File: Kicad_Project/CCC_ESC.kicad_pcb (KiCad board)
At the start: 4 copper layers, 99.9 x 82.6 mm, 160 parts, among them J1 Conn_01x07, J2 Conn_01x06, J3 Conn_01x06, J4 Conn_01x06, SW1 Conn_01x02, U1 NCP5183 / TF2190-TAH, U2 NCP5183 / TF2190-TAH, U3 NCP5183 / TF2190-TAH, U4 NCS20034DR2G, U5 STM32F401CCU6_Balckpill, U6 PQDE6W-Q110 / RD5-110S12W, U7 TO220_replacement_module

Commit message: initial layout approach
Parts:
- removed CX1, CX2, CX3, CX4, CX5, CX6, CX7, CX8: 470uF, CCC_ESC_Custom_parts:CAP_Polaryzed
- removed CX18, CX19, CX20, CX21, CX22, CX23, CX24, CX25, CX26, CX27, CX28, CX29, CX30, CX31, CX32: 4.7uF, Capacitor_SMD:C_1210_3225Metric
- removed PH2 (x2): PhasePad, TestPoint:TestPoint_THTPad_D4.0mm_Drill2.0mm
- removed TpVS1: TestPoint, TestPoint:TestPoint_THTPad_D2.0mm_Drill1.0mm
- added CD3: 4.7uF, Capacitor_SMD:C_1210_3225Metric, F.Cu at (86.2, 72.6)
- added CD4: 4.7uF, Capacitor_SMD:C_1210_3225Metric, F.Cu at (114.0, 72.6)
- added CD5: 4.7uF, Capacitor_SMD:C_1210_3225Metric, F.Cu at (118.2, 72.6)
- added CD6: 4.7uF, Capacitor_SMD:C_1210_3225Metric, F.Cu at (146.0, 72.6)
- added CS1: C, Capacitor_SMD:C_0805_2012Metric, F.Cu at (53.6, 81.6)
- added CS2: C, Capacitor_SMD:C_0805_2012Metric, F.Cu at (85.8, 81.7)
- added CS3: C, Capacitor_SMD:C_0805_2012Metric, F.Cu at (117.8, 81.7)
- added CX17: 4.7uF, Capacitor_SMD:C_1210_3225Metric, F.Cu at (67.2, 51.1)
- added NT3: NetTie_2, NetTie:NetTie-2_SMD_Pad0.5mm, F.Cu at (102.6, 88.5)
- added NT4: NetTie_2, NetTie:NetTie-2_SMD_Pad0.5mm, F.Cu at (102.6, 90.6)
- added NT5: NetTie_2, NetTie:NetTie-2_SMD_Pad0.5mm, F.Cu at (134.6, 88.5)
- added NT6: NetTie_2, NetTie:NetTie-2_SMD_Pad0.5mm, F.Cu at (134.6, 90.6)
- added PHA_1: PhasePad, TestPoint:my_2mm_slot, F.Cu at (59.3, 72.4)
- added PHA_2: PhasePad, TestPoint:my_2mm_slot, F.Cu at (76.1, 72.4)
- added PHB_1: PhasePad, TestPoint:my_2mm_slot, F.Cu at (91.8, 72.4)
- added PHB_2: PhasePad, TestPoint:my_2mm_slot, F.Cu at (108.3, 72.4)
- added PHC_1: PhasePad, TestPoint:my_2mm_slot, F.Cu at (123.6, 72.4)
- added PHC_2: PhasePad, TestPoint:my_2mm_slot, F.Cu at (140.3, 72.4)
- added QB1: NVMTSC4D3N15MC, Package_DFN_QFN:DFNW-8_L8.3-W8.4-P2.00-BL, F.Cu at (91.4, 64.6)
- added QB2: NVMTSC4D3N15MC, Package_DFN_QFN:DFNW-8_L8.3-W8.4-P2.00-BL, F.Cu at (91.3, 80.6)
- added QB3: NVMTSC4D3N15MC, Package_DFN_QFN:DFNW-8_L8.3-W8.4-P2.00-BL, F.Cu at (112.2, 64.6)
- added QB4: NVMTSC4D3N15MC, Package_DFN_QFN:DFNW-8_L8.3-W8.4-P2.00-BL, F.Cu at (101.7, 80.6)
- added QB5: NVMTSC4D3N15MC, Package_DFN_QFN:DFNW-8_L8.3-W8.4-P2.00-BL, F.Cu at (101.6, 64.6)
- added QB6: NVMTSC4D3N15MC, Package_DFN_QFN:DFNW-8_L8.3-W8.4-P2.00-BL, F.Cu at (112.1, 80.6)
- added QC1: NVMTSC4D3N15MC, Package_DFN_QFN:DFNW-8_L8.3-W8.4-P2.00-BL, F.Cu at (123.3, 64.6)
- added QC2: NVMTSC4D3N15MC, Package_DFN_QFN:DFNW-8_L8.3-W8.4-P2.00-BL, F.Cu at (123.4, 80.6)
- added QC3: NVMTSC4D3N15MC, Package_DFN_QFN:DFNW-8_L8.3-W8.4-P2.00-BL, F.Cu at (133.7, 64.6)
- added QC4: NVMTSC4D3N15MC, Package_DFN_QFN:DFNW-8_L8.3-W8.4-P2.00-BL, F.Cu at (133.8, 80.6)
- added QC5: NVMTSC4D3N15MC, Package_DFN_QFN:DFNW-8_L8.3-W8.4-P2.00-BL, F.Cu at (144.0, 64.6)
- added QC6: NVMTSC4D3N15MC, Package_DFN_QFN:DFNW-8_L8.3-W8.4-P2.00-BL, F.Cu at (144.1, 80.6)
- added REF**: CP_Radial_D18.0mm_P7.50mm, Capacitor_THT:CP_Radial_D18.0mm_P7.50mm, F.Cu at (57.3, 40.3)
- added REF**1: CP_Radial_D18.0mm_P7.50mm, Capacitor_THT:CP_Radial_D18.0mm_P7.50mm, F.Cu at (77.3, 40.3)
- added REF**2: CP_Radial_D18.0mm_P7.50mm, Capacitor_THT:CP_Radial_D18.0mm_P7.50mm, F.Cu at (97.3, 40.3)
- added REF**3: CP_Radial_D18.0mm_P7.50mm, Capacitor_THT:CP_Radial_D18.0mm_P7.50mm, F.Cu at (117.3, 40.3)
- added REF**4: CP_Radial_D18.0mm_P7.50mm, Capacitor_THT:CP_Radial_D18.0mm_P7.50mm, F.Cu at (137.3, 40.3)
- added RG10: 15R, Resistor_SMD:R_0603_1608Metric, F.Cu at (88.3, 87.2)
- added RG11: 15R, Resistor_SMD:R_0603_1608Metric, F.Cu at (96.6, 84.7)
- added RG12: 15R, Resistor_SMD:R_0603_1608Metric, F.Cu at (106.8, 84.6)
- added RG13: 15R, Resistor_SMD:R_0603_1608Metric, F.Cu at (117.9, 65.2)
- added RG14: 15R, Resistor_SMD:R_0603_1608Metric, F.Cu at (128.5, 67.9)
- added RG15: 15R, Resistor_SMD:R_0603_1608Metric, F.Cu at (138.8, 67.9)
- added RG16: 15R, Resistor_SMD:R_0603_1608Metric, F.Cu at (120.2, 87.2)
- added RG17: 15R, Resistor_SMD:R_0603_1608Metric, F.Cu at (128.6, 84.7)
- added RG18: 15R, Resistor_SMD:R_0603_1608Metric, F.Cu at (138.8, 84.6)
- added RG7: 15R, Resistor_SMD:R_0603_1608Metric, F.Cu at (86.0, 65.2)
- added RG8: 15R, Resistor_SMD:R_0603_1608Metric, F.Cu at (96.5, 67.9)
- added RG9: 15R, Resistor_SMD:R_0603_1608Metric, F.Cu at (106.8, 67.9)
- added RS1: R, Resistor_SMD:R_0805_2012Metric, F.Cu at (53.6, 78.0)
- added RS2: R, Resistor_SMD:R_0805_2012Metric, F.Cu at (85.8, 78.2)
- added RS3: R, Resistor_SMD:R_0805_2012Metric, F.Cu at (117.8, 78.2)
- added SHB1: 0.5mR, CCC_ESC_Custom_parts:Shunt_2512_6332Metric, F.Cu at (92.3, 89.8)
- added SHB2: 0.5mR, CCC_ESC_Custom_parts:Shunt_2512_6332Metric, F.Cu at (102.7, 89.8)
- added SHB3: 0.5mR, CCC_ESC_Custom_parts:Shunt_2512_6332Metric, F.Cu at (112.7, 89.8)
- added SHC1: 0.5mR, CCC_ESC_Custom_parts:Shunt_2512_6332Metric, F.Cu at (124.6, 89.6)
- added SHC2: 0.5mR, CCC_ESC_Custom_parts:Shunt_2512_6332Metric, F.Cu at (134.4, 89.6)
- added SHC3: 0.5mR, CCC_ESC_Custom_parts:Shunt_2512_6332Metric, F.Cu at (144.9, 89.6)
- added TpGND1: TestPoint, TestPoint:TestPoint_THTPad_D2.0mm_Drill1.0mm, F.Cu at (154.5, 77.9)
- added TpGND2: TestPoint, TestPoint:TestPoint_THTPad_D2.0mm_Drill1.0mm, F.Cu at (154.5, 81.9)
- added TpGND3: TestPoint, TestPoint:TestPoint_THTPad_D2.0mm_Drill1.0mm, F.Cu at (154.5, 86.0)
- added TpGS3: TestPoint, TestPoint:TestPoint_THTPad_D2.0mm_Drill1.0mm, F.Cu at (85.9, 59.0)
- added TpGS4: TestPoint, TestPoint:TestPoint_THTPad_D2.0mm_Drill1.0mm, F.Cu at (118.0, 58.9)
- added TpGS5: TestPoint, TestPoint:TestPoint_THTPad_D2.0mm_Drill1.0mm, F.Cu at (86.2, 89.9)
- added TpGS6: TestPoint, TestPoint:TestPoint_THTPad_D2.0mm_Drill1.0mm, F.Cu at (118.2, 89.9)
- QA1, QA2, QA3, QA4, QA5, QA6: value CRST030N10N -> NVMTSC4D3N15MC
- TpGS1, TpGS2: footprint TestPoint:TestPoint_THTPad_D1.5mm_Drill0.7mm -> TestPoint:TestPoint_THTPad_D2.0mm_Drill1.0mm
- moved CX17 14.4 mm to (50.4, 54.1), turned to 90 degrees
- moved R1 7.22 mm to (51.6, 66.0), turned to -90 degrees
- moved R3 7.03 mm to (148.4, 43.3), turned to 90 degrees
- moved R14 4.12 mm to (148.3, 47.1)
- moved TpGS1 4.09 mm to (53.4, 58.3)
- moved SW1 3.97 mm to (51.4, 82.6)
- moved R2 3.93 mm to (51.6, 62.3)
- moved TpGS2 3.47 mm to (56.1, 90.1)
- moved NT2 3.31 mm to (70.4, 90.5)
- moved CD2 3.23 mm to (81.7, 72.5)
- moved NT1 3.21 mm to (70.4, 88.4)
- moved RG2 3.21 mm to (64.2, 67.8)
- moved SHA3 3.21 mm to (70.4, 89.6)
- moved RG4 3.21 mm to (56.0, 87.0)
- moved SHA1 3.21 mm to (60.5, 89.6)
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- renumbered CX11 to CD1, CX13 to CD2, R43 to RG1, R55 to RG2, R61 to RG3, R44 to RG4, R56 to RG5, R62 to RG6
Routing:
- net /BU_GATESIG: track 17.3 -> 50.3 mm, vias 0 -> 3
- net VSENSE2: track 109.0 -> 80.3 mm, vias 6 -> 5
- net /CU_GATESIG: track 17.5 -> 44.1 mm, vias 0 -> 3
- net /CL_GATESIG: track 20.1 -> 40.1 mm, vias 0 -> 3
- net VSENSE: track 75.6 -> 56.4 mm, vias 3 -> 2
- net /BL_GATESIG: track 24.4 -> 40.1 mm, vias 1 -> 4
- net Net-(D7-A1): track 32.2 -> 37.7 mm, vias 0 -> 2
- net Net-(QC1-Pad1): track 0.00 -> 4.16 mm
- net Net-(QB1-Pad1): track 0.00 -> 4.16 mm
- net PHASE_B: track 17.3 -> 20.6 mm, vias 2 -> 90
- net Net-(QB6-Pad1): track 0.00 -> 2.69 mm
- net Net-(QC6-Pad1): track 0.00 -> 2.66 mm
- net Net-(QC4-Pad1): track 0.00 -> 2.49 mm
- net Net-(QB4-Pad1): track 0.00 -> 2.44 mm
- net Net-(QC5-Pad1): track 0.00 -> 2.28 mm
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- added copper zone on F.Cu, net Net-(NT3-Pad1)
- added copper zone on F.Cu, net Net-(NT5-Pad1)
- added copper zone on B.Cu, net PHASE_A
- added copper zone on B.Cu, net PHASE_B
- added copper zone on F.Cu, net PHASE_B
- added copper zone on B.Cu, net PHASE_C
- added copper zone on F.Cu, net PHASE_C
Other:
- board size 99.9 x 82.6 mm -> 102.4 x 87.7 mm
- board text added: "CD1"

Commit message: general layout complete
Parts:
- removed CD2, CD3: 4.7uF, Capacitor_SMD:C_1210_3225Metric
- added ?: , , F.Cu at (62.9, 56.1)
- added ?: , , F.Cu at (127.1, 55.9)
- added ?: , , F.Cu at (91.3, 56.2)
- added REF**: MountingHole_2.5mm_Pad, MountingHole:MountingHole_2.5mm_Pad, F.Cu at (84.2, 72.3)
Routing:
- net VBAT: vias 218 -> 210
- net PHASE_C: vias 90 -> 66
- net PHASE_B: vias 90 -> 66
- net PHASE_A: vias 106 -> 82
- net GND: vias 326 -> 320
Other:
- board text added: "MOUNTING HOLES FOR HEAT SINK DONT BREAK UP VBUS PLANE UP TOP CRAM IN SOME CERAMICS"

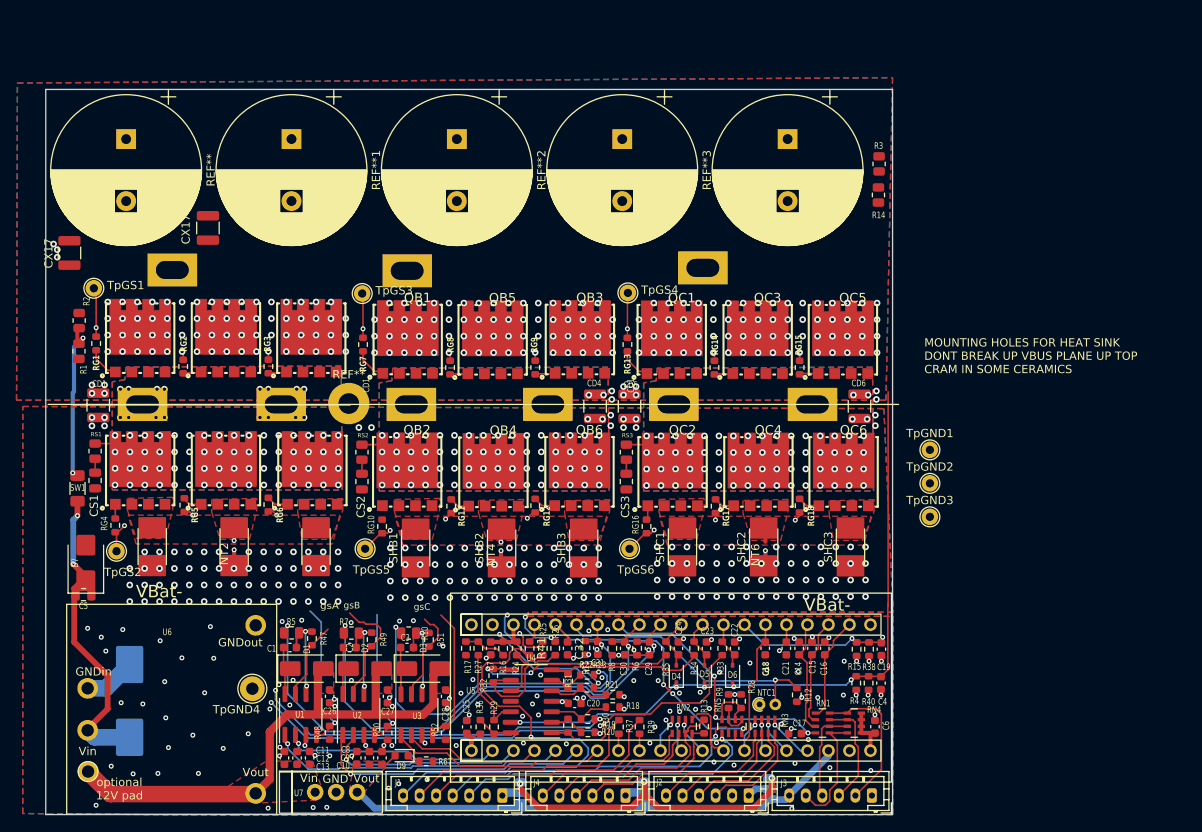
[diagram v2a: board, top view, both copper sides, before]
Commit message: reversed side of bus bars
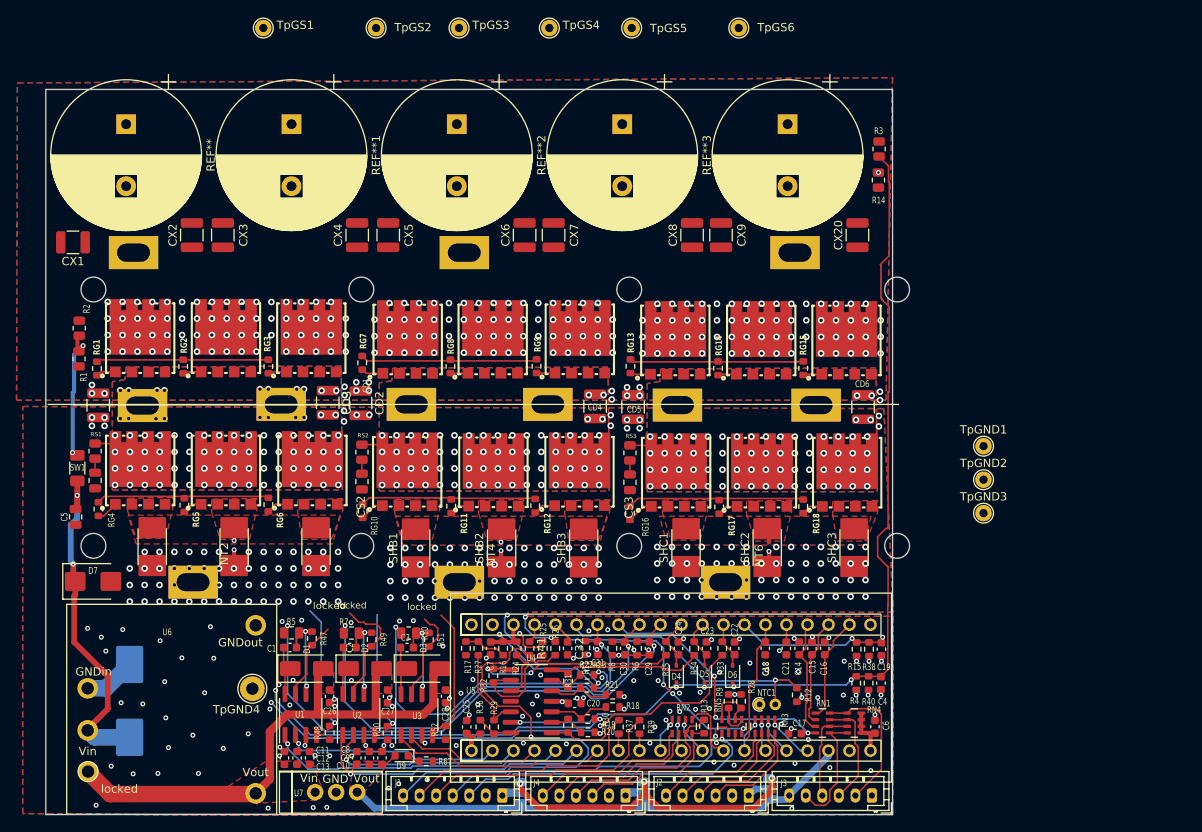
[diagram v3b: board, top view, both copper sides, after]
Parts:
- removed the ? at (127.1, 55.9)
- removed CX17 (x2): 4.7uF, Capacitor_SMD:C_1210_3225Metric
- removed the REF** at (84.2, 72.3)
- added 1: , , B.Cu at (98.2, 54.0)
- added 2: , , B.Cu at (138.2, 54.0)
- added 3: , , B.Cu at (97.6, 93.9)
- added 4: , , B.Cu at (129.8, 93.9)
- added CD2: 4.7uF, Capacitor_SMD:C_1210_3225Metric, F.Cu at (85.7, 72.2)
- added CD3: 4.7uF, Capacitor_SMD:C_1210_3225Metric, F.Cu at (81.7, 72.2)
- added CX1: 4.7uF, Capacitor_SMD:C_1210_3225Metric, F.Cu at (50.9, 52.8)
- added CX2: 4.7uF, Capacitor_SMD:C_1210_3225Metric, F.Cu at (65.2, 51.9)
- added CX20: 4.7uF, Capacitor_SMD:C_1210_3225Metric, F.Cu at (145.8, 51.9)
- added CX3: 4.7uF, Capacitor_SMD:C_1210_3225Metric, F.Cu at (69.0, 51.9)
- added CX4: 4.7uF, Capacitor_SMD:C_1210_3225Metric, F.Cu at (85.2, 51.9)
- added CX5: 4.7uF, Capacitor_SMD:C_1210_3225Metric, F.Cu at (89.0, 51.9)
- added CX6: 4.7uF, Capacitor_SMD:C_1210_3225Metric, F.Cu at (105.5, 51.9)
- added CX7: 4.7uF, Capacitor_SMD:C_1210_3225Metric, F.Cu at (109.0, 51.9)
- added CX8: 4.7uF, Capacitor_SMD:C_1210_3225Metric, F.Cu at (125.8, 51.9)
- added CX9: 4.7uF, Capacitor_SMD:C_1210_3225Metric, F.Cu at (129.2, 51.9)
- ? (x2), PHA_1, PHA_2, PHB_1, PHB_2, PHC_1, PHC_2: moved to B.Cu
- moved TpGS5 70.8 mm to (118.4, 26.9)
- moved TpGS2 70.6 mm to (87.5, 26.9)
- moved TpGS6 64.4 mm to (131.4, 26.9)
- moved ? 37.8 mm to (65.4, 93.9), turned to 180 degrees
- moved TpGS1 37.6 mm to (73.9, 26.9)
- moved TpGS3 34.2 mm to (97.6, 26.9)
- moved TpGS4 33.4 mm to (108.5, 26.9)
- moved ? 33.2 mm to (58.2, 54.0), turned to 180 degrees
- moved QB3 10.5 mm to (101.6, 64.6)
- moved QB5 10.5 mm to (112.2, 64.5)
- moved C5 9.45 mm to (51.2, 86.0), turned to -90 degrees
- moved TpGND1 6.50 mm to (161.0, 77.5)
- moved TpGND2 6.50 mm to (161.0, 81.5)
- moved TpGND3 6.50 mm to (161.0, 85.5)
- moved RG1 3.03 mm to (53.8, 68.0)
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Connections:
- ? pad 1: PHASE_A -> GND
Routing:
- net VSENSE2: track 80.3 -> 111.4 mm
- net VSENSE: track 56.4 -> 75.2 mm, vias 2 -> 3
- net /AU_GATESIG: track 45.9 -> 30.3 mm, vias 3 -> 0
- net /BU_GATESIG: track 50.3 -> 35.2 mm, vias 3 -> 0
- net /CU_GATESIG: track 44.1 -> 32.4 mm, vias 3 -> 0
- net /AL_GATESIG: track 43.1 -> 38.8 mm, vias 4 -> 1
- net Net-(SW1-Pin_2): track 19.5 -> 16.2 mm
- net Net-(QB2-Pad1): track 0.00 -> 3.00 mm
- net Net-(D7-A1): track 37.7 -> 40.6 mm
- net /BL_GATESIG: track 40.1 -> 38.1 mm, vias 4 -> 1
- net /CL_GATESIG: track 40.1 -> 38.1 mm, vias 3 -> 0
- net Net-(QA1-Pad1): track 4.16 -> 2.39 mm
- net Net-(QC1-Pad1): track 4.16 -> 2.49 mm
- net Net-(QA2-Pad1): track 1.81 -> 3.35 mm
- net Net-(QC2-Pad1): track 1.74 -> 3.26 mm
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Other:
- board size 102.4 x 87.7 mm -> 104.5 x 87.7 mm
- board text added: "locked"
- board text added: "with great thanks to: github.com/badgineer/MP2-ESC"
- board text removed: "-"
- board text removed: "3V3"
- board text removed: "5V"
- board text removed: "MOUNTING HOLES FOR HEAT SINK DONT BREAK UP VBUS PLANE UP TOP CRAM IN SOME CERAMICS"
- board text removed: "MP2-ESC v0.4"
- board text removed: "github.com/badgineer/MP2-ESC"
- board text removed: "gsA"
- board text removed: "gsB"
- board text removed: "gsC"
- board text removed: "optional 12V pad"

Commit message: reversed side of bus bars
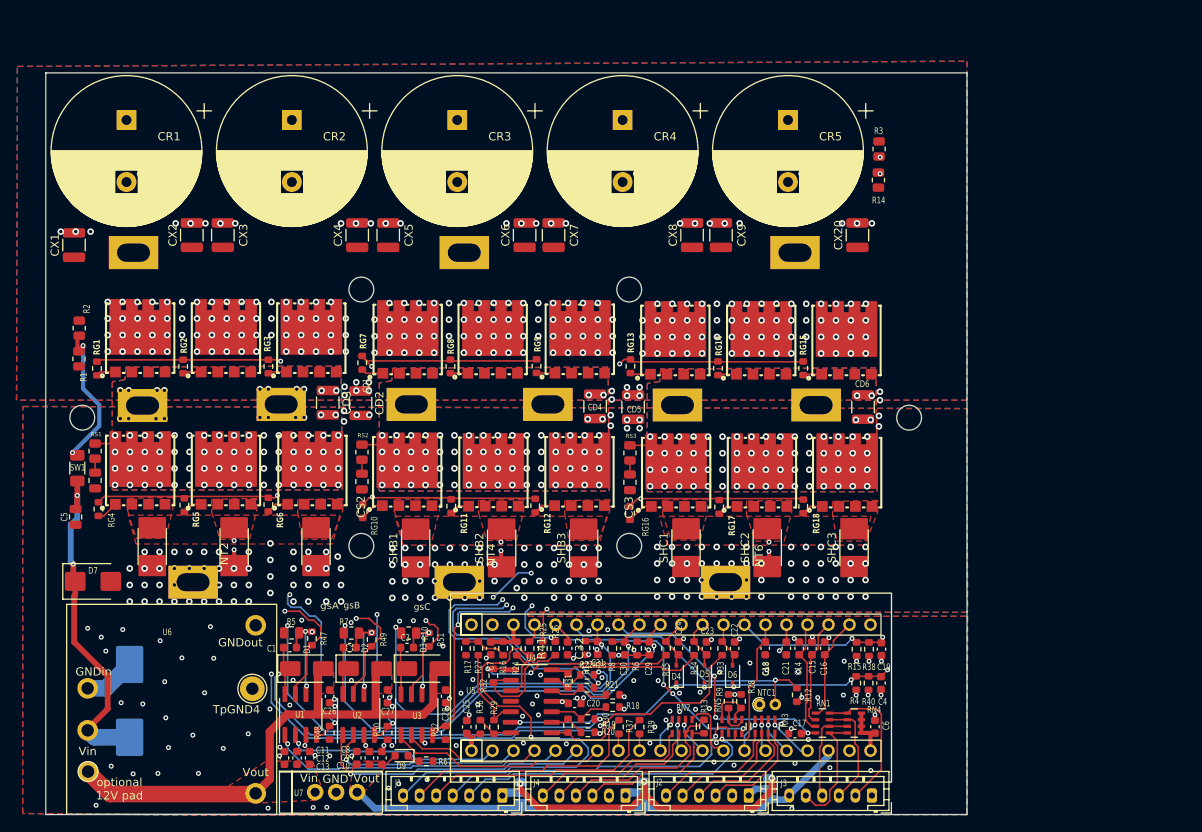
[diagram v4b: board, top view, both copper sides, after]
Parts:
- removed CD1: 4.7uF, Capacitor_SMD:C_1210_3225Metric
- removed REF**, REF**1, REF**2, REF**3, REF**4: CP_Radial_D18.0mm_P7.50mm, Capacitor_THT:CP_Radial_D18.0mm_P7.50mm
- removed TpGND1, TpGND2, TpGND3, TpGS1, TpGS2, TpGS3, TpGS4, TpGS5, TpGS6: TestPoint, TestPoint:TestPoint_THTPad_D2.0mm_Drill1.0mm
- added CR1: 470uF, Capacitor_THT:CP_Radial_D18.0mm_P7.50mm, F.Cu at (57.4, 38.0)
- added CR2: 470uF, Capacitor_THT:CP_Radial_D18.0mm_P7.50mm, F.Cu at (77.3, 38.0)
- added CR3: 470uF, Capacitor_THT:CP_Radial_D18.0mm_P7.50mm, F.Cu at (97.3, 38.0)
- added CR4: 470uF, Capacitor_THT:CP_Radial_D18.0mm_P7.50mm, F.Cu at (117.3, 38.0)
- added CR5: 470uF, Capacitor_THT:CP_Radial_D18.0mm_P7.50mm, F.Cu at (137.3, 38.0)
- moved CX1 0.35 mm to (51.0, 53.1), turned to 90 degrees
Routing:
- net /CU_GATESIG: track 32.4 -> 85.4 mm, vias 0 -> 2
- net /AU_GATESIG: track 30.3 -> 71.0 mm, vias 0 -> 2
- net PHASE_C: track 18.7 -> 54.3 mm, vias 66 -> 68
- net A_SHC_V-: track 7.65 -> 42.4 mm
- net /BU_GATESIG: track 35.2 -> 69.4 mm, vias 0 -> 2
- net /CL_GATESIG: track 38.1 -> 72.0 mm, vias 0 -> 3
- net A_SHC_V+: track 9.50 -> 42.3 mm, vias 1 -> 2
- net A_SHB_V+: track 17.4 -> 37.4 mm
- net /AL_GATESIG: track 38.8 -> 57.2 mm, vias 1 -> 3
- net A_SHB_V-: track 22.2 -> 40.3 mm
- net PHASE_A: track 21.7 -> 37.2 mm, vias 82 -> 83
- net PHASE_B: track 20.6 -> 35.3 mm
- net /BL_GATESIG: track 38.1 -> 52.6 mm, vias 1 -> 3
- net A_SHA_V-: track 52.9 -> 65.9 mm
- net A_SHA_V+: track 52.6 -> 64.9 mm
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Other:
- board size 104.5 x 87.7 mm -> 111.4 x 89.7 mm
- board text added: "-"
- board text added: "3V3"
- board text added: "5V"
- board text added: "gsA"
- board text added: "gsB"
- board text added: "gsC"
- board text added: "optional 12V pad"
- board text removed: "locked"
